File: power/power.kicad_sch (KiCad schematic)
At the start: 179 parts, among them J1 USB-C Power + USB2.0, J2 USB, J3 BATTERY OUT, J4 BACKUP, J5 I2C, Q1 SI7617DN-T1-GE3, Q2 CSD18534Q5A, Q3 CSD18534Q5A, Q4 CSD18534Q5A, Q5 CSD18534Q5A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

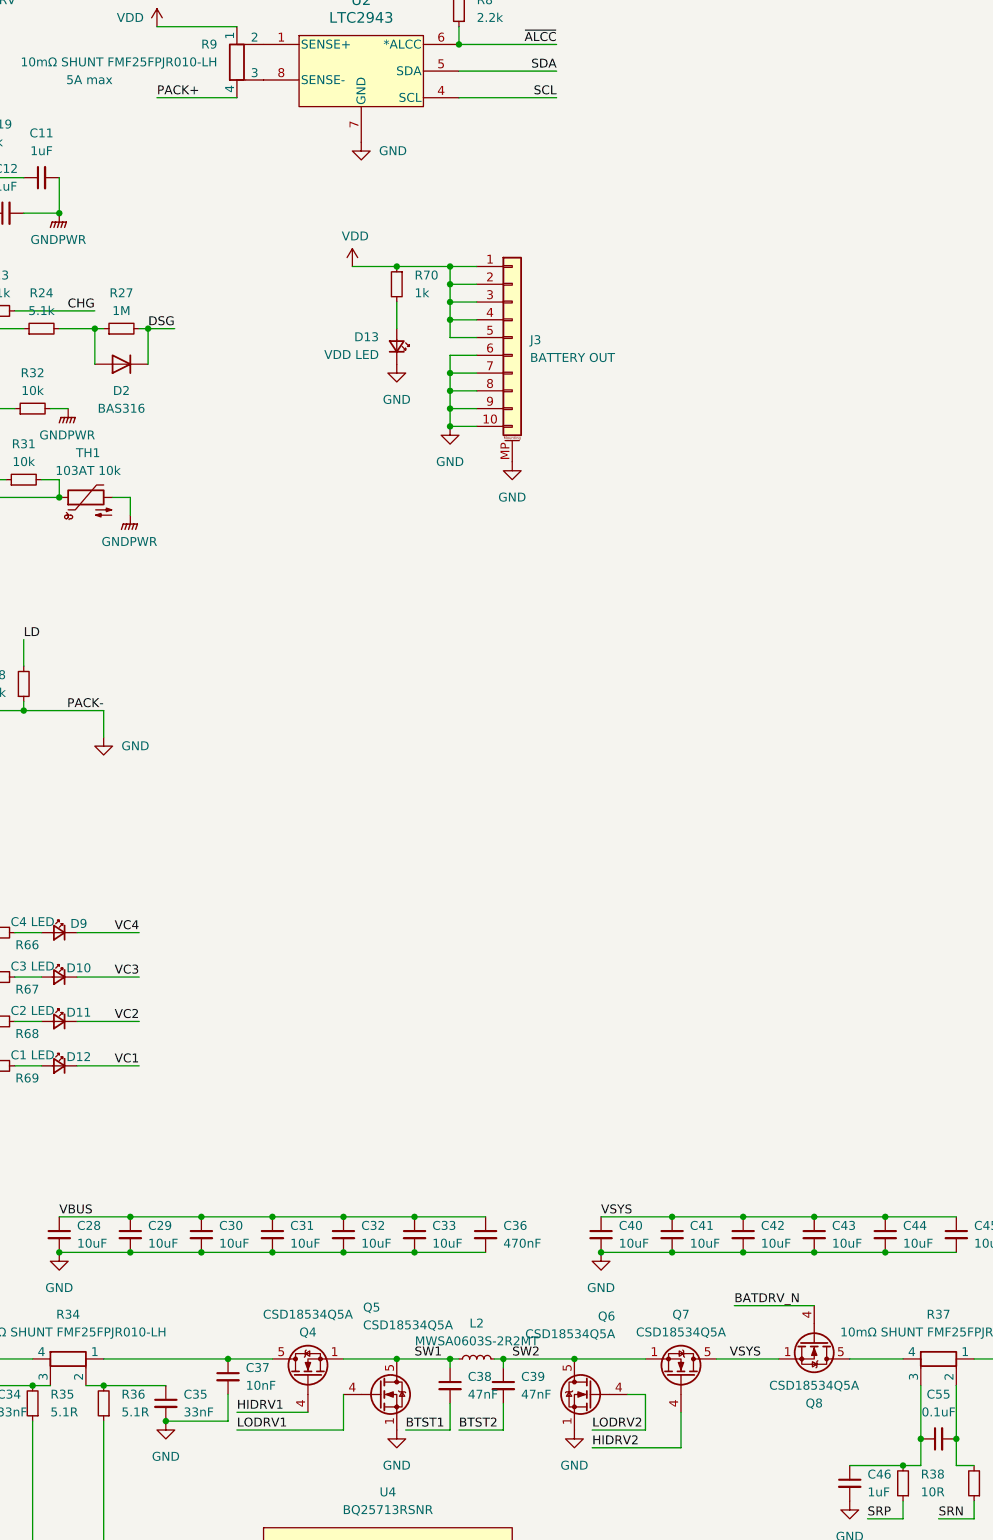
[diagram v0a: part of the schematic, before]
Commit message: powertrain charging functional (balancing difficult to test)
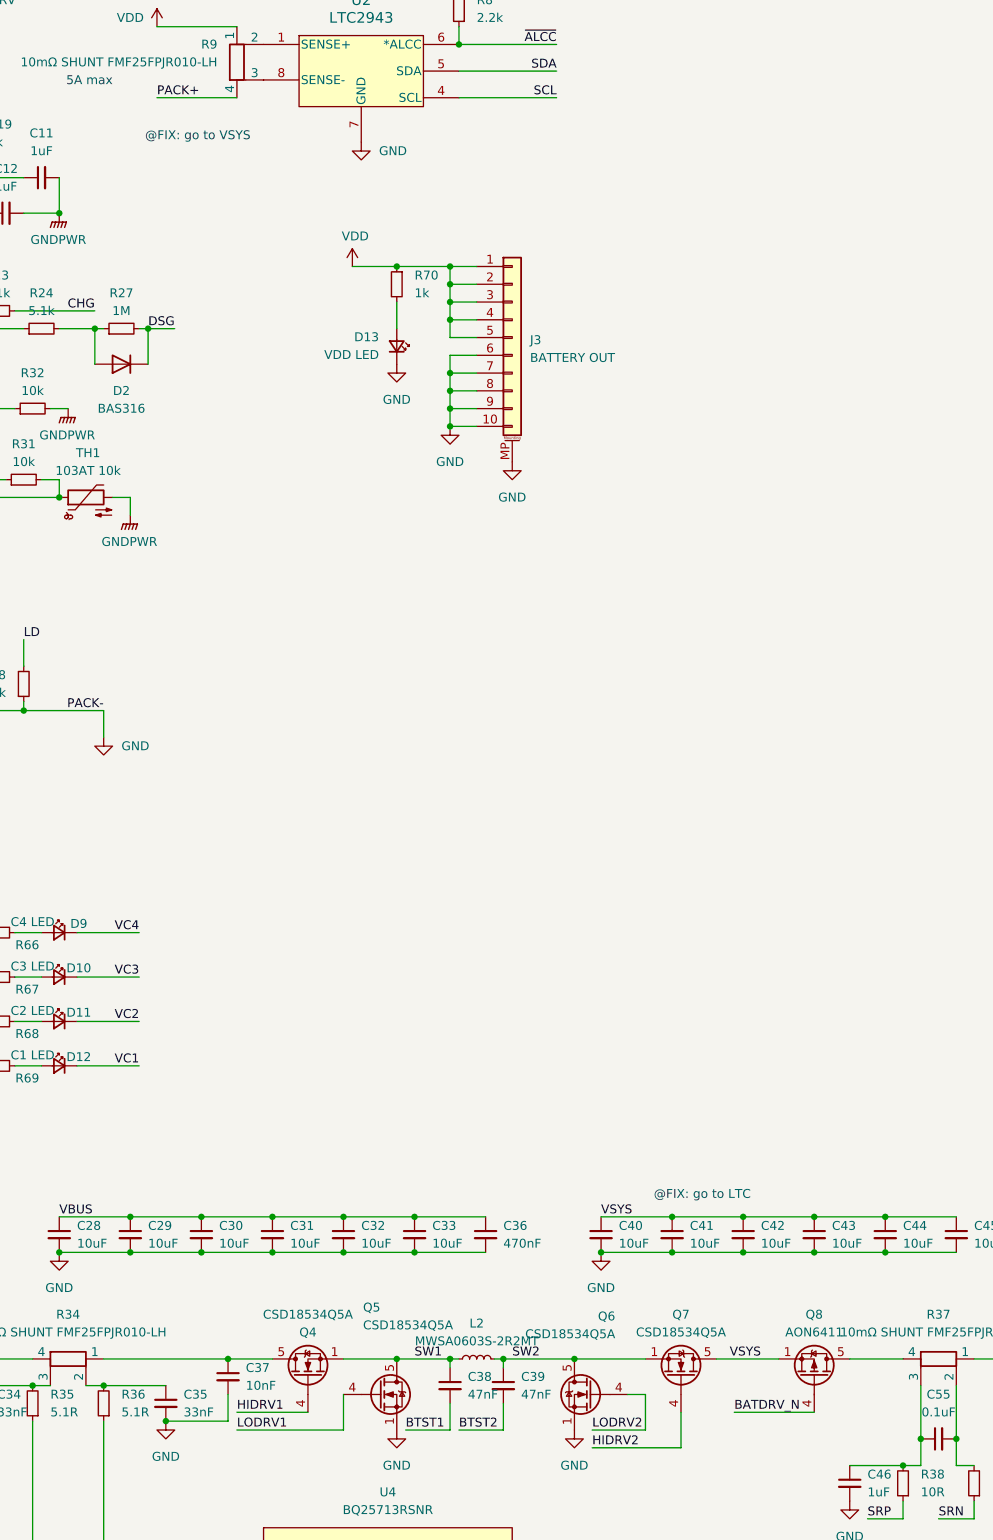
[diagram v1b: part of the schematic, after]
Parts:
- removed Q8: CSD18534Q5A, Package_TO_SOT_SMD:TDSON-8-1, symbol Transistor_FET:CSD18534Q5A
- added Q8: AON6411, Package_DFN_QFN:AO_DFN-8-1EP_5.55x5.2mm_P1.27mm_EP4.12x4.6mm, symbol Transistor_FET:AON6411
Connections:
- net BATDRV_N: now also Q8.4 (G)
- net VSYS: now also Q8.1 (S), Q8.2 (S), Q8.3 (S)
- net at R37.4: now also Q8.5 (D)
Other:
- note added: "@FIX: go to LTC"
- note added: "@FIX: go to VSYS"
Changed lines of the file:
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@@
 	(generator_version "8.99")
 	(paper "A4")
+	(text "@FIX: go to VSYS"
+		(exclude_from_sim no)
+		(at 221.742 51.308 0)
+		(effects
+			(font
+				(size 1.27 1.27)
+			)
+		)
+	)
 	(text "hystersis"
 		(exclude_from_sim no)
@@
 		)
 	)
+	(text "@FIX: go to LTC"
+		(exclude_from_sim no)
+		(at 293.878 202.692 0)
+		(effects
+			(font
+				(size 1.27 1.27)
+			)
+		)
+	)
 	(text "ILIM = 2.9A"
 		(exclude_from_sim no)
@@
 	(wire
 		(pts
-			(xy 298.45 218.44) (xy 309.88 218.44)
+			(xy 298.45 233.68) (xy 309.88 233.68)
 		)
 		(stroke
@@
 	)
 	(label "BATDRV_N"
-		(at 298.45 218.44 0)
+		(at 298.45 233.68 0)
 		(fields_autoplaced yes)
 		(effects
@@
 	)
 	(symbol
+		(lib_id "Transistor_FET:AON6411")
+		(at 309.88 228.6 270)
+		(mirror x)
+		(unit 1)
+		(exclude_from_sim no)
+		(in_bom yes)
+		(on_board yes)
+		(dnp no)
+		(fields_autoplaced yes)
+		(property "Reference" "Q8"
+			(at 309.88 219.71 90)
+			(effects
+				(font
+					(size 1.27 1.27)
+				)
+			)
+		)
+		(property "Value" "AON6411"
+			(at 309.88 222.25 90)
+			(effects
+				(font
+					(size 1.27 1.27)
+				)
+			)
+		)
+		(property "Footprint" "Package_DFN_QFN:AO_DFN-8-1EP_5.55x5.2mm_P1.27mm_EP4.12x4.6mm"
+			(at 307.975 223.52 0)
+			(effects
+				(font
+					(size 1.27 1.27)
+				)
+				(justify left)
+				(hide yes)
+			)
+		)
+		(property "Datasheet" "http://www.aosmd.com/res/data_sheets/AON6411.pdf"
+			(at 306.07 223.52 0)
+			(effects
+				(font
+					(size 1.27 1.27)
+				)
+				(justify left)
+				(hide yes)
+			)
+		)
+		(property "Description" "-85A Id, -20V Vds, P-Channel MOSFET, DFN-8"
+			(at 309.88 228.6 0)
+			(effects
+				(font
+					(size 1.27 1.27)
+				)
+				(hide yes)
+			)
+		)
+		(pin "4"
+		)
+		(pin "2"
+		)
+		(pin "3"
+		)
+		(pin "5"
+		)
+		(pin "1"
+		)
+		(instances
+			(project ""
+				(path "/f6ef1cf7-e202-4cf7-a9a2-de51d726791c"
+					(reference "Q8")
+					(unit 1)
+				)
+			)
+		)
+	)
+	(symbol
 		(lib_id "Device:R_Small")
 		(at 128.27 116.84 180)
@@
 					(unit 1)
 				)
-			)
-		)
-	)
-	(symbol
-		(lib_id "Transistor_FET:CSD18534Q5A")
-		(at 309.88 223.52 270)
-		(unit 1)
-		(exclude_from_sim no)
-		(in_bom yes)
-		(on_board yes)
-		(dnp no)
-		(property "Reference" "Q8"
-			(at 309.88 232.41 90)
-			(effects
-				(font
-					(size 1.27 1.27)
-				)
-			)
-		)
-		(property "Value" "CSD18534Q5A"
-			(at 309.88 229.87 90)
-			(effects
-				(font
-					(size 1.27 1.27)
-				)
-			)
-		)
-		(property "Footprint" "Package_TO_SOT_SMD:TDSON-8-1"
-			(at 307.975 228.6 0)
-			(effects
-				(font
-					(size 1.27 1.27)
-					(italic yes)
-				)
-				(justify left)
-				(hide yes)
-			)
-		)
-		(property "Datasheet" "http://www.ti.com/lit/gpn/csd18534q5a"
-			(at 306.07 228.6 0)
-			(effects
-				(font
-					(size 1.27 1.27)
-				)
-				(justify left)
-				(hide yes)
-			)
-		)
-		(property "Description" "50A Id, 60V Vds, NexFET N-Channel Power MOSFET, 9.8mOhm Ron, 17nC Qg(typ), SON8 5x6mm"
-			(at 309.88 223.52 0)
-			(effects
-				(font
-					(size 1.27 1.27)
-				)
-				(hide yes)
-			)
-		)
-		(property "LCSC" "C115943"
-			(at 309.88 232.41 0)
-			(effects
-				(font
-					(size 1.27 1.27)
-				)
-				(hide yes)
-			)
-		)
-		(pin "1"
-		)
-		(pin "2"
-		)
-		(pin "3"
-		)
-		(pin "4"
-		)
-		(pin "5"
-		)
-		(instances
-			(project "power"
-				(path "/f6ef1cf7-e202-4cf7-a9a2-de51d726791c"
-					(reference "Q8")
-					(unit 1)
-				)
